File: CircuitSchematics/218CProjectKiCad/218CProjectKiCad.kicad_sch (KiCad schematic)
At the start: 19 parts, among them M1 Motor, SW1 Reset, U3 TiVa

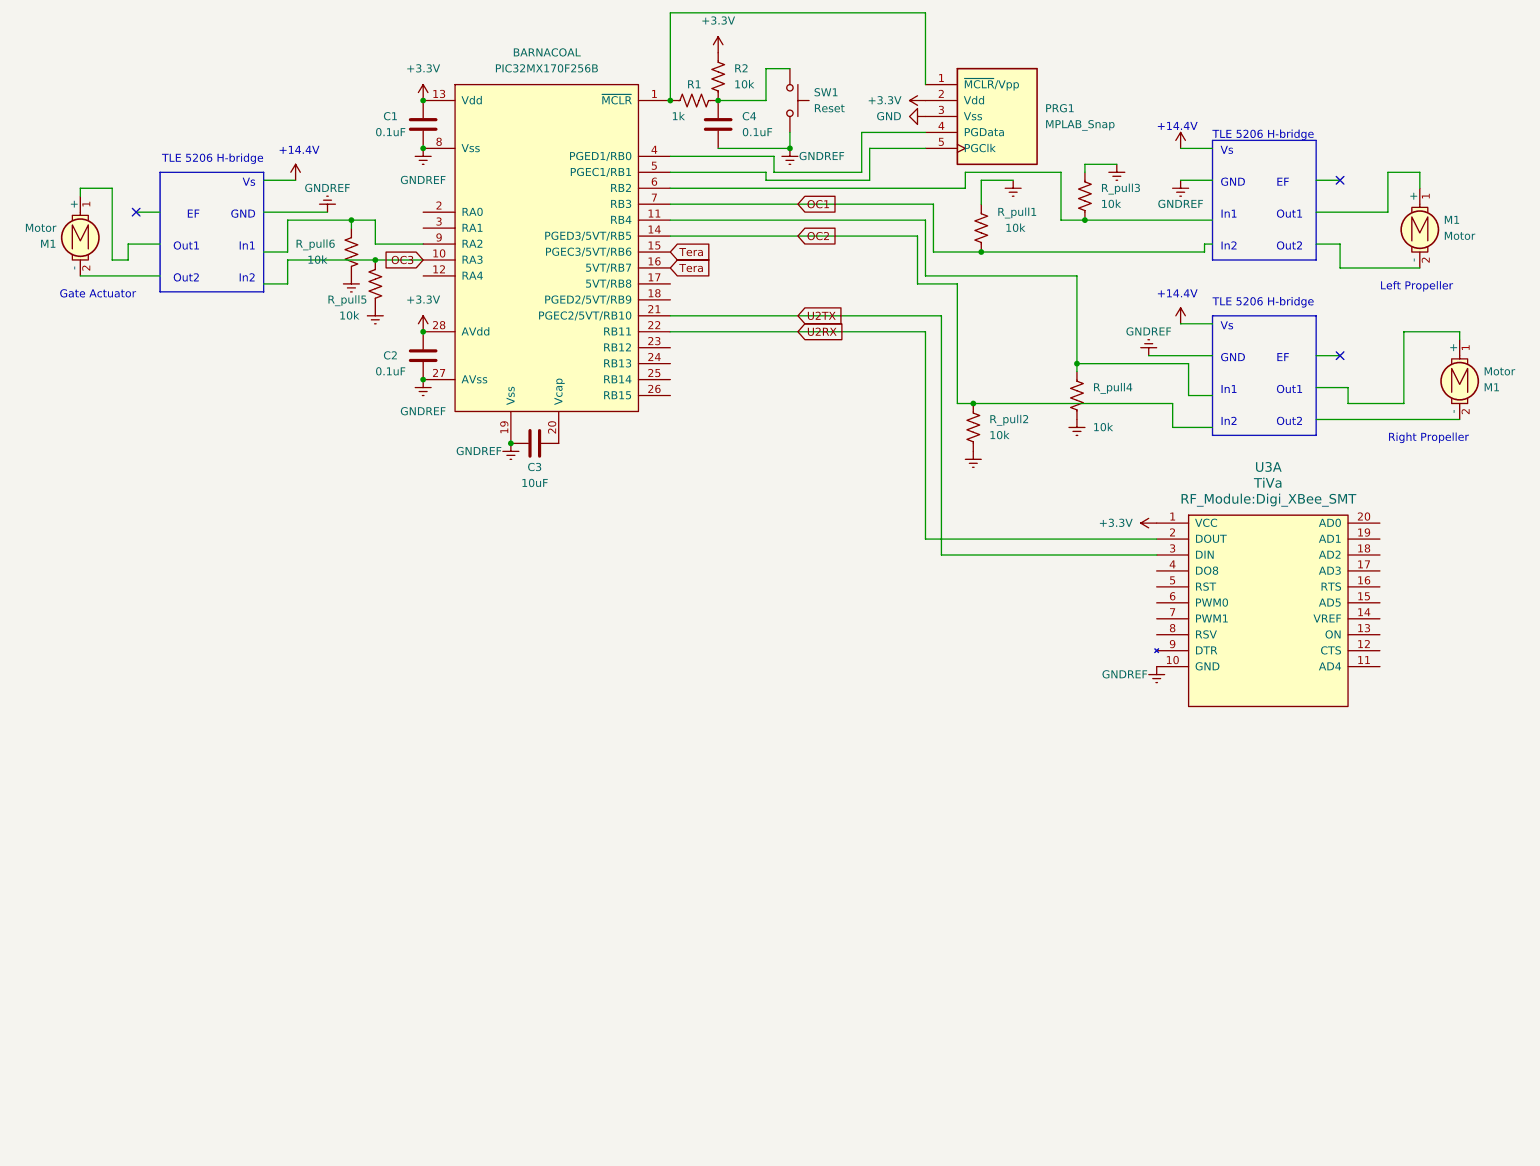
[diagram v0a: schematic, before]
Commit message: Finished implementing ControllerComm.c TX
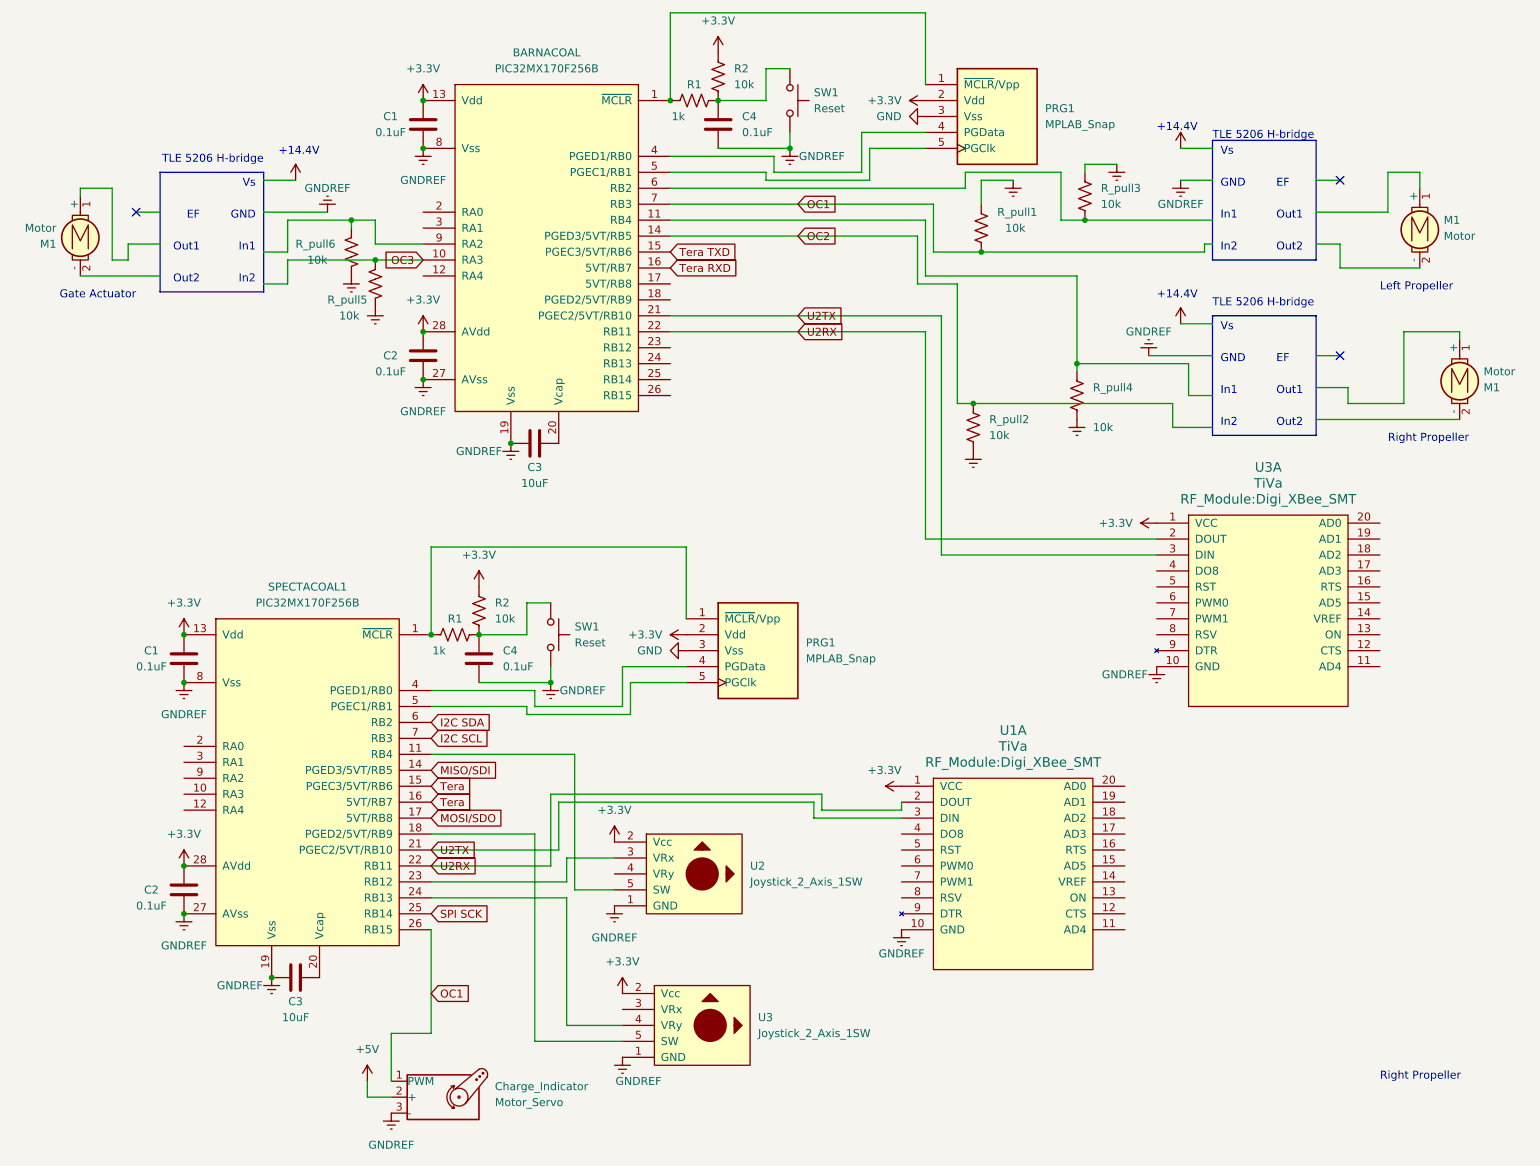
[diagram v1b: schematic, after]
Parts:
- added C1, C2, C4: 0.1uF, symbol ME218_BaseLib:Cap
- added C3: 10uF, symbol ME218_BaseLib:Cap
- added Charge_Indicator: Motor_Servo, symbol ME218_BaseLib:Motor_Servo
- added PRG1: MPLAB_Snap, symbol ME218_BaseLib:MPLAB_Snap
- added R1: 1k, symbol ME218_BaseLib:Res1
- added R2: 10k, symbol ME218_BaseLib:Res1
- added SPECTACOAL1: PIC32MX170F256B, symbol ME218_BaseLib:PIC32MX170F256B
- added SW1: Reset, symbol ME218_BaseLib:SW-PB
- added U1: TiVa, RF_Module:Digi_XBee_SMT, symbol ME218_BaseLib:TiVa
- added U2, U3: Joystick_2_Axis_1SW, symbol ME218_BaseLib:Joystick_2_Axis_1SW
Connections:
- net +3.3V: now also C1.1, C2.1, PRG1.2 (Vdd), R2.1, SPECTACOAL1.13 (Vdd), SPECTACOAL1.28 (AVdd), U1.1 (VCC), U2.2 (Vcc), U3.2 (Vcc)
- net GND: now also PRG1.3 (Vss)
- net GNDREF: now also C1.2, C2.2, C3.1, C4.2, Charge_Indicator.3 (-), SPECTACOAL1.19 (Vss), SPECTACOAL1.27 (AVss), SPECTACOAL1.8 (Vss), SW1.2, U1.10 (GND), U2.1 (GND), U3.1 (GND)
- net OC1: now also Charge_Indicator.1 (PWM), SPECTACOAL1.26 (RB15)
- net Tera: now also SPECTACOAL1.15 (PGEC3/5VT/RB6), SPECTACOAL1.16 (5VT/RB7); no longer BARNACOAL.15 (PGEC3/5VT/RB6), BARNACOAL.16 (5VT/RB7)
- net U2RX: now also SPECTACOAL1.22 (RB11), U1.2 (DOUT)
- net U2TX: now also SPECTACOAL1.21 (PGEC2/5VT/RB10), U1.3 (DIN)
- new net: C3.2, SPECTACOAL1.20 (Vcap)
- new net: C4.1, R1.1, R2.2, SW1.1
- new net: SPECTACOAL1.24 (RB13), U3.4 (VRy)
- new net: SPECTACOAL1.18 (PGED2/5VT/RB9), U3.5 (SW)
- new net: PRG1.1 (~{MCLR}/Vpp), R1.2, SPECTACOAL1.1 (~{MCLR})
- new net: PRG1.4 (PGData), SPECTACOAL1.4 (PGED1/RB0)
- new net: PRG1.5 (PGClk), SPECTACOAL1.5 (PGEC1/RB1)
- new net: SPECTACOAL1.11 (RB4), U2.5 (SW)
- new net: SPECTACOAL1.23 (RB12), U2.3 (VRx)
- new net +5V: Charge_Indicator.2 (+)
- new net I2C SCL: SPECTACOAL1.7 (RB3)
- new net I2C SDA: SPECTACOAL1.6 (RB2)
- new net MISO/SDI: SPECTACOAL1.14 (PGED3/5VT/RB5)
- new net MOSI/SDO: SPECTACOAL1.17 (5VT/RB8)
- new net SPI SCK: SPECTACOAL1.25 (RB14)
- new net Tera RXD: BARNACOAL.16 (5VT/RB7)
- new net Tera TXD: BARNACOAL.15 (PGEC3/5VT/RB6)
